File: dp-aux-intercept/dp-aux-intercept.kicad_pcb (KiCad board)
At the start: 2 copper layers, 24 parts

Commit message: Small fixes.
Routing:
- net /DCFG2: track 7.76 -> 14.6 mm
- net /DCFG1: track 4.83 -> 11.0 mm
- net /DHPD: track 32.4 -> 34.9 mm
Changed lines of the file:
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@@
-(kicad_pcb (version 4) (host pcbnew 0.201506030104+5696~23~ubuntu14.04.1-product)
+(kicad_pcb (version 4) (host pcbnew 0.201506252249+5822~23~ubuntu14.04.1-product)
   (general
     (links 86)
@@
     (thickness 1.6)
     (drawings 2)
-    (tracks 570)
+    (tracks 583)
     (zones 0)
     (modules 24)
@@
   (segment (start 42.418 70.74408) (end 42.418 63.73876) (width 0.15) (layer F.Cu) (net 3))
   (segment (start 45.20692 73.533) (end 42.418 70.74408) (width 0.15) (layer F.Cu) (net 3))
+  (segment (start 31.742 32.31) (end 32.467001 33.035001) (width 0.15) (layer F.Cu) (net 4))
+  (segment (start 32.467001 33.035001) (end 36.083001 33.035001) (width 0.15) (layer F.Cu) (net 4))
+  (segment (start 36.083001 33.035001) (end 36.78399 33.73599) (width 0.15) (layer F.Cu) (net 4))
+  (segment (start 36.78399 33.73599) (end 36.78399 34.24399) (width 0.15) (layer F.Cu) (net 4))
+  (segment (start 36.78399 34.24399) (end 36.83 34.29) (width 0.15) (layer F.Cu) (net 4))
   (segment (start 35.1917 51.43246) (end 34.1757 51.43246) (width 0.15) (layer F.Cu) (net 4))
   (segment (start 35.1917 55.24246) (end 35.1917 51.43246) (width 0.15) (layer F.Cu) (net 4))
+  (segment (start 37.084 34.036) (end 37.338 34.29) (width 0.15) (layer F.Cu) (net 5))
+  (segment (start 37.084 33.578998) (end 37.084 34.036) (width 0.15) (layer F.Cu) (net 5))
+  (segment (start 32.242 30.81) (end 33.016999 31.584999) (width 0.15) (layer F.Cu) (net 5))
+  (segment (start 33.016999 31.584999) (end 35.090001 31.584999) (width 0.15) (layer F.Cu) (net 5))
+  (segment (start 35.090001 31.584999) (end 37.084 33.578998) (width 0.15) (layer F.Cu) (net 5))
   (segment (start 37.7317 51.43246) (end 36.643099 50.343859) (width 0.15) (layer F.Cu) (net 5))
   (segment (start 36.643099 50.343859) (end 34.230099 50.343859) (width 0.15) (layer F.Cu) (net 5))
   (segment (start 37.7317 55.24246) (end 37.7317 54.021146) (width 0.15) (layer F.Cu) (net 5))
   (segment (start 37.7317 54.021146) (end 37.7317 51.43246) (width 0.15) (layer F.Cu) (net 5))
+  (segment (start 36.322 33.87402) (end 36.322 34.29) (width 0.15) (layer F.Cu) (net 6))
+  (segment (start 36.25798 33.81) (end 36.322 33.87402) (width 0.15) (layer F.Cu) (net 6))
+  (segment (start 34.242 33.81) (end 36.25798 33.81) (width 0.15) (layer F.Cu) (net 6))
   (segment (start 40.2717 51.43246) (end 38.820301 49.981061) (width 0.15) (layer F.Cu) (net 6))
   (segment (start 38.820301 49.981061) (end 34.669171 49.981061) (width 0.15) (layer F.Cu) (net 6))

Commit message: Temp commit.
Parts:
- RCCFG1: renamed from RCCFG2; value 5M -> 1M
- RCCFG2: renamed from RCHPD1; value 100K -> 5M
- RCHPD1: renamed from RCCFG1; value 1M -> 100K
- RDCFG1: renamed from RDCFG2; value 5M -> 1M
- RDCFG2: renamed from RDHPD1; value 100K -> 5M
- RDHPD1: renamed from RDCFG1; value 1M -> 100K
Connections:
- net Net-(JCCFG1-Pad2) renamed /JCHPD
- net Net-(JCCFG1-Pad4) renamed /JCCFG1
- net Net-(JCCFG1-Pad6) renamed /JCCFG2
- net Net-(JDCFG1-Pad2) renamed /JDHPD
- net Net-(JDCFG1-Pad4) renamed /JDCFG1
- net Net-(JDCFG1-Pad6) renamed /JDCFG2
- JCCFG1 pad 1: /CCFG1 -> /CHPD
- JCCFG1 pad 3: /CCFG2 -> /CCFG1
- JCCFG1 pad 5: /CHPD -> /CCFG2
- JDCFG1 pad 1: /DCFG1 -> /DHPD
- JDCFG1 pad 3: /DCFG2 -> /DCFG1
- JDCFG1 pad 5: /DHPD -> /DCFG2
- PCFG1 pad 1: /CCFG1 -> /CHPD
- PCFG1 pad 2: /DCFG1 -> /DHPD
- PCFG1 pad 3: /CCFG2 -> /CCFG1
- PCFG1 pad 4: /DCFG2 -> /DCFG1
- PCFG1 pad 5: /CHPD -> /CCFG2
- PCFG1 pad 6: /DHPD -> /DCFG2
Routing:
- net /DHPD: track 34.9 -> 50.9 mm
- net /DCFG1: track 11.0 -> 26.7 mm
- net /DCFG2: track 14.6 -> 29.0 mm
- net /CHPD: track 17.8 -> 28.3 mm
- net VDD: track 112.8 -> 116.5 mm
- net /CCFG2: track 6.74 -> 10.3 mm
- net /CCFG1: track 6.21 -> 9.25 mm

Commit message: Temp commit.
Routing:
- net /DAUX1_P: track 47.1 -> 44.8 mm
- net /DAUX1_N: track 50.6 -> 48.6 mm
- net VDD: track 116.5 -> 118.3 mm
- net /DCFG2: track 29.0 -> 29.6 mm, vias 0 -> 1
- net /DCFG1: track 26.7 -> 27.0 mm, vias 0 -> 1

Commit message: More temp commit.
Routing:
- net /CCFG1: track 9.25 -> 33.6 mm
- net /CCFG2: track 10.3 -> 34.2 mm
- net /CHPD: track 28.3 -> 26.9 mm
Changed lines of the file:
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@@
   (general
     (links 86)
-    (no_connects 29)
+    (no_connects 30)
     (area 22.242 18.23 58.531921 98.968)
     (thickness 1.6)
     (drawings 2)
-    (tracks 593)
+    (tracks 607)
     (zones 0)
     (modules 24)
@@
   (gr_line (start 32.004 82.55) (end 32.004 34.798) (layer B.SilkS) (width 0.2))
   (gr_line (start 32.004 34.798) (end 32.004 82.55) (layer F.SilkS) (width 0.2))
+  (segment (start 36.280301 71.403421) (end 36.280301 63.043859) (width 0.15) (layer F.Cu) (net 1))
+  (segment (start 32.467001 84.312999) (end 34.540003 84.312999) (width 0.15) (layer F.Cu) (net 1))
+  (segment (start 38.745549 77.395093) (end 38.745549 73.868669) (width 0.15) (layer F.Cu) (net 1))
+  (segment (start 36.957 78.1685) (end 37.435419 77.690081) (width 0.15) (layer F.Cu) (net 1))
+  (segment (start 36.280301 63.043859) (end 36.868101 62.456059) (width 0.15) (layer F.Cu) (net 1))
+  (segment (start 34.540003 84.312999) (end 36.957 81.896002) (width 0.15) (layer F.Cu) (net 1))
+  (segment (start 36.957 81.896002) (end 36.957 78.1685) (width 0.15) (layer F.Cu) (net 1))
+  (segment (start 31.742 85.038) (end 32.467001 84.312999) (width 0.15) (layer F.Cu) (net 1))
+  (segment (start 36.868101 62.456059) (end 37.7317 61.59246) (width 0.15) (layer F.Cu) (net 1))
+  (segment (start 37.435419 77.690081) (end 38.450561 77.690081) (width 0.15) (layer F.Cu) (net 1))
+  (segment (start 38.450561 77.690081) (end 38.745549 77.395093) (width 0.15) (layer F.Cu) (net 1))
+  (segment (start 38.745549 73.868669) (end 36.280301 71.403421) (width 0.15) (layer F.Cu) (net 1))
   (segment (start 37.7317 61.59246) (end 37.7317 57.78246) (width 0.15) (layer B.Cu) (net 1))
-  (segment (start 35.8394 83.693) (end 35.8394 82.9056) (width 0.15) (layer F.Cu) (net 1))
-  (segment (start 35.219401 84.312999) (end 35.8394 83.693) (width 0.15) (layer F.Cu) (net 1))
-  (segment (start 31.742 85.038) (end 32.467001 84.312999) (width 0.15) (layer F.Cu) (net 1))
-  (segment (start 32.467001 84.312999) (end 35.219401 84.312999) (width 0.15) (layer F.Cu) (net 1))
+  (segment (start 32.242 86.538) (end 33.016999 85.763001) (width 0.15) (layer F.Cu) (net 2))
+  (segment (start 33.016999 85.763001) (end 35.090001 85.763001) (width 0.15) (layer F.Cu) (net 2))
+  (segment (start 35.090001 85.763001) (end 37.353919 83.499083) (width 0.15) (layer F.Cu) (net 2))
+  (segment (start 37.353919 78.315999) (end 37.525919 78.143999) (width 0.15) (layer F.Cu) (net 2))
+  (segment (start 37.353919 83.499083) (end 37.353919 78.315999) (width 0.15) (layer F.Cu) (net 2))
+  (segment (start 37.525919 78.143999) (end 38.696001 78.143999) (width 0.15) (layer F.Cu) (net 2))
+  (segment (start 39.045559 77.794441) (end 39.045559 76.035079) (width 0.15) (layer F.Cu) (net 2))
+  (segment (start 38.696001 78.143999) (end 39.045559 77.794441) (width 0.15) (layer F.Cu) (net 2))
+  (segment (start 39.045559 76.035079) (end 39.24808 75.832558) (width 0.15) (layer F.Cu) (net 2))
+  (segment (start 39.24808 75.832558) (end 39.24554 75.830018) (width 0.15) (layer F.Cu) (net 2))
+  (segment (start 39.0017 62.86246) (end 40.2717 61.59246) (width 0.15) (layer F.Cu) (net 2))
+  (segment (start 39.24554 75.830018) (end 39.24554 65.45834) (width 0.15) (layer F.Cu) (net 2))
+  (segment (start 39.24554 65.45834) (end 39.0017 65.2145) (width 0.15) (layer F.Cu) (net 2))
+  (segment (start 39.0017 65.2145) (end 39.0017 62.86246) (width 0.15) (layer F.Cu) (net 2))
   (segment (start 40.2717 57.78246) (end 40.2717 61.59246) (width 0.15) (layer B.Cu) (net 2))
-  (segment (start 36.195 84.658002) (end 36.195 82.8802) (width 0.15) (layer F.Cu) (net 2))
-  (segment (start 32.242 86.538) (end 32.967001 85.812999) (width 0.15) (layer F.Cu) (net 2))
-  (segment (start 32.967001 85.812999) (end 35.040003 85.812999) (width 0.15) (layer F.Cu) (net 2))
-  (segment (start 35.040003 85.812999) (end 36.195 84.658002) (width 0.15) (layer F.Cu) (net 2))
   (segment (start 42.164 60.325) (end 42.164 70.49008) (width 0.15) (layer F.Cu) (net 3))
   (segment (start 42.164 70.49008) (end 45.20692 73.533) (width 0.15) (layer F.Cu) (net 3))
@@
   (segment (start 35.1917 57.78246) (end 35.1917 58.79606) (width 0.15) (layer F.Cu) (net 3))
   (segment (start 35.1917 58.79606) (end 35.83164 59.436) (width 0.15) (layer F.Cu) (net 3))
-  (segment (start 35.249799 83.038001) (end 35.3822 82.9056) (width 0.15) (layer F.Cu) (net 3))
-  (segment (start 34.242 83.538) (end 34.741999 83.038001) (width 0.15) (layer F.Cu) (net 3))
-  (segment (start 34.741999 83.038001) (end 35.249799 83.038001) (width 0.15) (layer F.Cu) (net 3))
   (segment (start 35.1917 61.59246) (end 35.1917 57.78246) (width 0.15) (layer F.Cu) (net 3))
   (segment (start 35.7505 33.5915) (end 36.643099 34.484099) (width 0.15) (layer F.Cu) (net 4))
   (segment (start 36.643099 34.484099) (end 36.643099 34.992099) (width 0.15) (layer F.Cu) (net 4))
+  (segment (start 36.643099 34.992099) (end 36.50742 35.127778) (width 0.15) (layer F.Cu) (net 4))
+  (segment (start 36.50742 35.127778) (end 36.50742 50.20818) (width 0.15) (layer F.Cu) (net 4))
+  (segment (start 36.50742 50.20818) (end 37.7317 51.43246) (width 0.15) (layer F.Cu) (net 4))
   (segment (start 31.742 32.31) (end 32.467001 33.035001) (width 0.15) (layer B.Cu) (net 4))
   (segment (start 32.467001 33.035001) (end 35.194001 33.035001) (width 0.15) (layer B.Cu) (net 4))
   (segment (start 35.194001 33.035001) (end 35.7505 33.5915) (width 0.15) (layer B.Cu) (net 4))
   (via (at 35.7505 33.5915) (size 0.6) (drill 0.3) (layers F.Cu B.Cu) (net 4))
-  (segment (start 36.643099 50.343859) (end 37.7317 51.43246) (width 0.15) (layer F.Cu) (net 4))
-  (segment (start 36.643099 34.992099) (end 36.643099 50.343859) (width 0.15) (layer F.Cu) (net 4))
   (segment (start 37.7317 55.24246) (end 37.7317 54.021146) (width 0.15) (layer F.Cu) (net 4))
   (segment (start 37.7317 54.021146) (end 37.7317 51.43246) (width 0.15) (layer F.Cu) (net 4))
-  (segment (start 36.634438 33.129436) (end 39.0144 35.509398) (width 0.15) (layer F.Cu) (net 5))
-  (segment (start 36.6395 32.3215) (end 36.6395 32.745764) (width 0.15) (layer F.Cu) (net 5))
-  (segment (start 36.6395 32.745764) (end 36.634438 32.750826) (width 0.15) (layer F.Cu) (net 5))
-  (segment (start 36.634438 32.750826) (end 36.634438 33.129436) (width 0.15) (layer F.Cu) (net 5))
+  (segment (start 36.6395 32.3215) (end 36.6395 33.134498) (width 0.15) (layer F.Cu) (net 5))
+  (segment (start 36.6395 33.134498) (end 39.0144 35.509398) (width 0.15) (layer F.Cu) (net 5))
+  (segment (start 39.0144 35.509398) (end 39.0144 50.17516) (width 0.15) (layer F.Cu) (net 5))
+  (segment (start 39.0144 50.17516) (end 40.2717 51.43246) (width 0.15) (layer F.Cu) (net 5))
   (segment (start 36.6395 32.131) (end 36.6395 32.3215) (width 0.15) (layer B.Cu) (net 5))
   (via (at 36.6395 32.3215) (size 0.6) (drill 0.3) (layers F.Cu B.Cu) (net 5))
@@
   (segment (start 32.242 30.81) (end 33.016999 31.584999) (width 0.15) (layer B.Cu) (net 5))
   (segment (start 33.016999 31.584999) (end 36.093499 31.584999) (width 0.15) (layer B.Cu) (net 5))
-  (segment (start 39.0144 35.509398) (end 39.0144 50.17516) (width 0.15) (layer F.Cu) (net 5))
-  (segment (start 39.0144 50.17516) (end 40.2717 51.43246) (width 0.15) (layer F.Cu) (net 5))
   (segment (start 40.2717 55.24246) (end 40.2717 51.43246) (width 0.15) (layer F.Cu) (net 5))
   (segment (start 47.74692 73.533) (end 46.658319 72.444399) (width 0.15) (layer F.Cu) (net 6))
@@
   (segment (start 32.742 83.538) (end 35.254 81.026) (width 0.15) (layer F.Cu) (net 17))
   (segment (start 35.254 81.026) (end 35.97892 81.026) (width 0.15) (layer F.Cu) (net 17))
-  (segment (start 32.742 33.81) (end 32.742 34.517106) (width 0.15) (layer F.Cu) (net 18))
-  (segment (start 32.742 34.517106) (end 31.92749 35.331616) (width 0.15) (layer F.Cu) (net 18))
-  (segment (start 31.92749 35.331616) (end 31.92749 35.496166) (width 0.15) (layer F.Cu) (net 18))
   (segment (start 33.340896 75.606729) (end 31.9025 74.168333) (width 0.125) (layer F.Cu) (net 18))
   (segment (start 31.9025 74.168333) (end 31.9025 35.496166) (width 0.125) (layer F.Cu) (net 18))
+  (segment (start 31.92749 35.331616) (end 31.92749 35.496166) (width 0.15) (layer F.Cu) (net 18))
+  (segment (start 32.742 34.517106) (end 31.92749 35.331616) (width 0.15) (layer F.Cu) (net 18))
+  (segment (start 32.742 33.81) (end 32.742 34.517106) (width 0.15) (layer F.Cu) (net 18))
   (segment (start 37.35056 76.67008) (end 37.52056 76.84008) (width 0.15) (layer F.Cu) (net 18))
   (segment (start 35.53206 76.67008) (end 37.35056 76.67008) (width 0.15) (layer F.Cu) (net 18))
@@
   (segment (start 32.016999 34.108003) (end 32.016999 33.461999) (width 0.15) (layer F.Cu) (net 20))
   (segment (start 32.016999 33.461999) (end 32.516999 32.961999) (width 0.15) (layer F.Cu) (net 20))
+  (segment (start 33.71386 30.83814) (end 33.742 30.81) (width 0.15) (layer F.Cu) (net 20))
   (segment (start 32.516999 32.961999) (end 32.516999 31.961999) (width 0.15) (layer F.Cu) (net 20))
-  (segment (start 32.516999 31.961999) (end 33.168999 31.309999) (width 0.15) (layer F.Cu) (net 20))
-  (segment (start 33.168999 31.309999) (end 33.242001 31.309999) (width 0.15) (layer F.Cu) (net 20))
-  (segment (start 33.242001 31.309999) (end 33.742 30.81) (width 0.15) (layer F.Cu) (net 20))
+  (segment (start 33.640858 30.83814) (end 33.71386 30.83814) (width 0.15) (layer F.Cu) (net 20))
+  (segment (start 32.516999 31.961999) (end 33.640858 30.83814) (width 0.15) (layer F.Cu) (net 20))
   (segment (start 31.5975 74.294667) (end 31.5975 35.369834) (width 0.125) (layer F.Cu) (net 20))
   (segment (start 33.125229 75.822396) (end 31.5975 74.294667) (width 0.125) (layer F.Cu) (net 20))

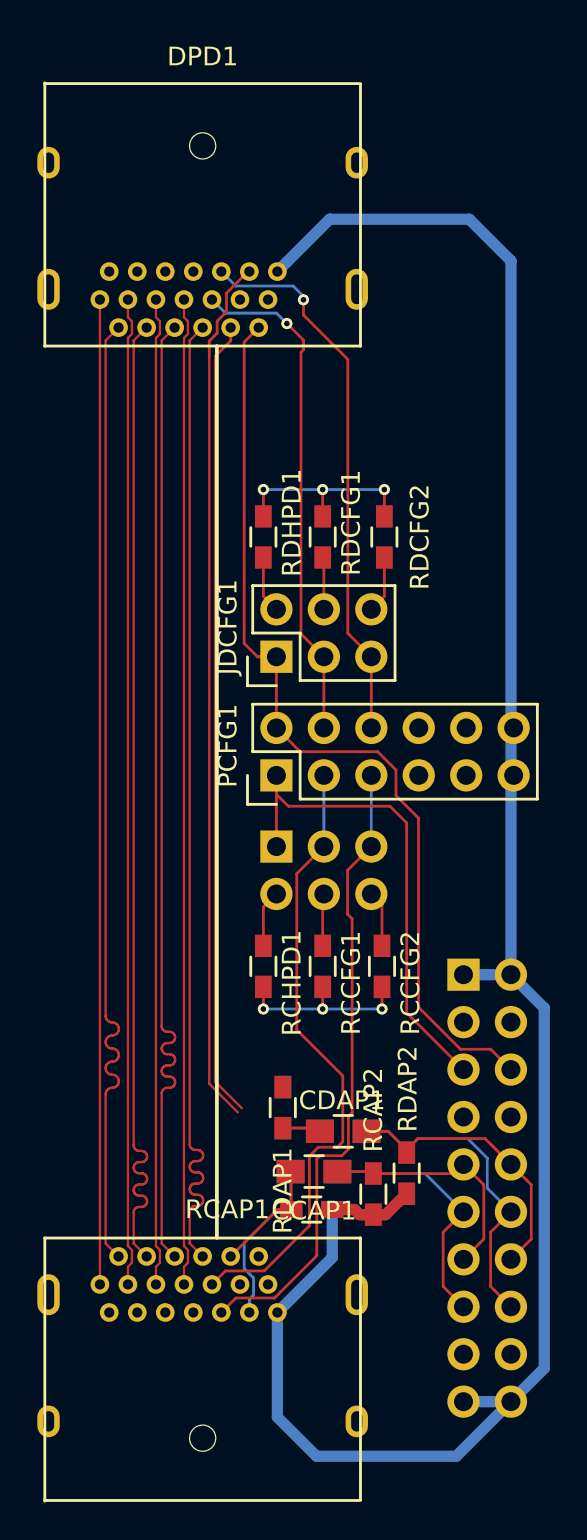
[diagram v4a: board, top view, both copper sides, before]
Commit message: Finishing connecting the traces.
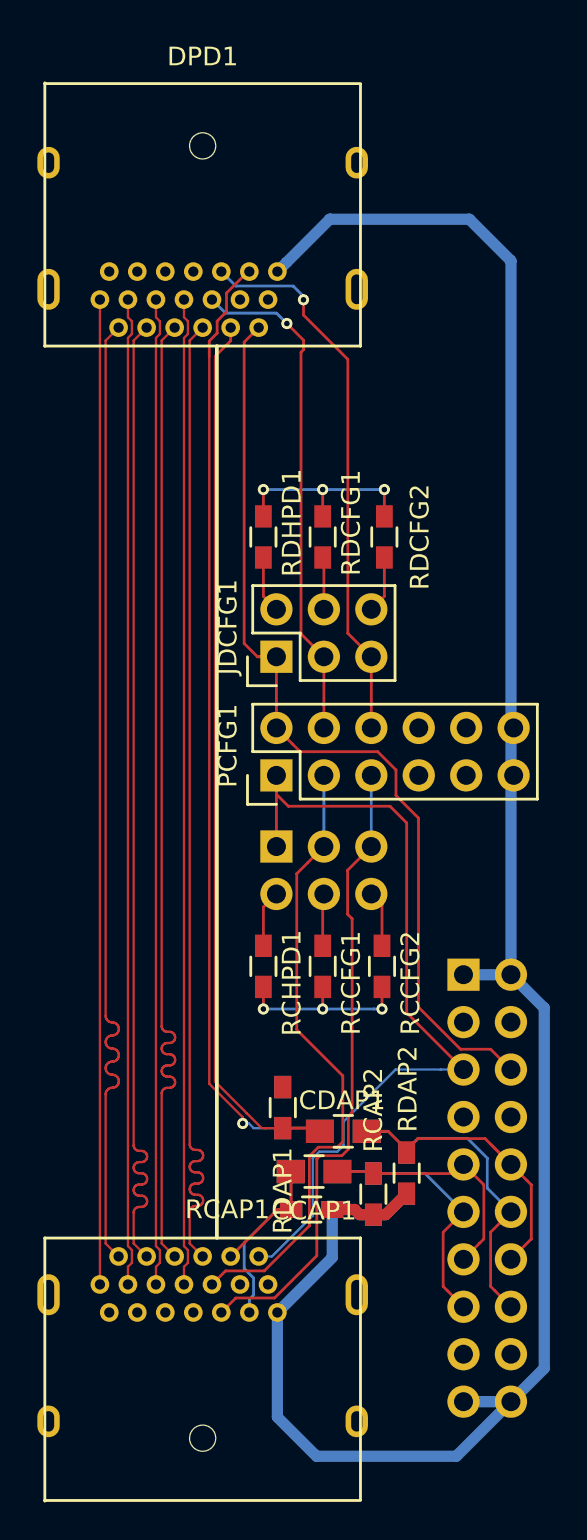
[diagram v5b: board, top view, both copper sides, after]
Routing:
- net /CHPD: track 26.9 -> 44.6 mm
- net /DAUX1_N: track 48.6 -> 51.6 mm, vias 0 -> 1
- net /DAUX1_P: track 44.8 -> 47.4 mm
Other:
- net class Default: trace_width 0.15 -> 0.125
- rule trace_min: 0.15 -> 0.125
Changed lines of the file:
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@@
-(kicad_pcb (version 4) (host pcbnew 0.201506252249+5822~23~ubuntu14.04.1-product)
+(kicad_pcb (version 4) (host pcbnew 4.0.2+e4-6225~38~ubuntu14.04.1-stable)
   (general
     (links 86)
-    (no_connects 30)
+    (no_connects 29)
     (area 22.242 18.23 58.531921 98.968)
     (thickness 1.6)
     (drawings 2)
-    (tracks 607)
+    (tracks 626)
     (zones 0)
     (modules 24)
@@
   (page A4)
   (layers
-    (0 F.Cu signal)
+    (0 F.Cu signal hide)
     (31 B.Cu signal)
     (32 B.Adhes user)
@@
   )
   (setup
-    (last_trace_width 0.15)
+    (last_trace_width 0.125)
+    (user_trace_width 0.125)
+    (user_trace_width 0.15)
     (trace_clearance 0.15)
     (zone_clearance 0.508)
     (zone_45_only no)
-    (trace_min 0.15)
+    (trace_min 0.125)
     (segment_width 0.2)
     (edge_width 0.1)
@@
   (net_class Default "This is the default net class."
     (clearance 0.15)
-    (trace_width 0.15)
+    (trace_width 0.125)
     (via_dia 0.6)
     (via_drill 0.3)
@@
   (segment (start 39.0017 65.2145) (end 39.0017 62.86246) (width 0.15) (layer F.Cu) (net 2))
   (segment (start 40.2717 57.78246) (end 40.2717 61.59246) (width 0.15) (layer B.Cu) (net 2))
+  (segment (start 34.242 83.538) (end 34.949106 83.538) (width 0.125) (layer B.Cu) (net 3))
+  (segment (start 34.949106 83.538) (end 37.1348 81.352306) (width 0.125) (layer B.Cu) (net 3))
+  (segment (start 37.1348 81.352306) (end 37.1348 78.2828) (width 0.125) (layer B.Cu) (net 3))
+  (segment (start 38.4556 77.9272) (end 38.7858 77.597) (width 0.125) (layer B.Cu) (net 3))
+  (segment (start 43.985606 73.533) (end 45.20692 73.533) (width 0.125) (layer B.Cu) (net 3))
+  (segment (start 37.1348 78.2828) (end 37.4904 77.9272) (width 0.125) (layer B.Cu) (net 3))
+  (segment (start 38.7858 77.597) (end 38.7858 76.317338) (width 0.125) (layer B.Cu) (net 3))
+  (segment (start 37.4904 77.9272) (end 38.4556 77.9272) (width 0.125) (layer B.Cu) (net 3))
+  (segment (start 38.7858 76.317338) (end 41.570138 73.533) (width 0.125) (layer B.Cu) (net 3))
+  (segment (start 41.570138 73.533) (end 43.985606 73.533) (width 0.125) (layer B.Cu) (net 3))
   (segment (start 42.164 60.325) (end 42.164 70.49008) (width 0.15) (layer F.Cu) (net 3))
   (segment (start 42.164 70.49008) (end 45.20692 73.533) (width 0.15) (layer F.Cu) (net 3))
@@
   (segment (start 32.742 83.538) (end 35.254 81.026) (width 0.15) (layer F.Cu) (net 17))
   (segment (start 35.254 81.026) (end 35.97892 81.026) (width 0.15) (layer F.Cu) (net 17))
-  (segment (start 33.340896 75.606729) (end 31.9025 74.168333) (width 0.125) (layer F.Cu) (net 18))
-  (segment (start 31.9025 74.168333) (end 31.9025 35.496166) (width 0.125) (layer F.Cu) (net 18))
+  (segment (start 33.601479 75.867079) (end 34.40448 76.67008) (width 0.125) (layer F.Cu) (net 18))
+  (segment (start 34.40448 76.67008) (end 35.53206 76.67008) (width 0.125) (layer F.Cu) (net 18))
+  (segment (start 33.601246 75.867079) (end 33.601479 75.867079) (width 0.125) (layer F.Cu) (net 18))
+  (segment (start 31.9025 35.496166) (end 31.9025 74.168333) (width 0.125) (layer F.Cu) (net 18))
+  (segment (start 31.9025 74.168333) (end 33.601246 75.867079) (width 0.125) (layer F.Cu) (net 18))
   (segment (start 31.92749 35.331616) (end 31.92749 35.496166) (width 0.15) (layer F.Cu) (net 18))
   (segment (start 32.742 34.517106) (end 31.92749 35.331616) (width 0.15) (layer F.Cu) (net 18))
@@
   (segment (start 33.467001 82.814199) (end 35.2552 81.026) (width 0.15) (layer B.Cu) (net 19))
   (segment (start 35.2552 81.026) (end 35.97892 81.026) (width 0.15) (layer B.Cu) (net 19))
+  (segment (start 33.385579 76.418621) (end 33.721454 76.418621) (width 0.125) (layer B.Cu) (net 20))
+  (segment (start 33.721454 76.418621) (end 33.972913 76.67008) (width 0.125) (layer B.Cu) (net 20))
+  (segment (start 33.972913 76.67008) (end 34.625678 76.67008) (width 0.125) (layer B.Cu) (net 20))
+  (segment (start 34.625678 76.67008) (end 35.53206 76.67008) (width 0.125) (layer B.Cu) (net 20))
+  (segment (start 33.385579 76.082746) (end 33.385579 76.418621) (width 0.125) (layer F.Cu) (net 20))
+  (via (at 33.385579 76.418621) (size 0.6) (drill 0.3) (layers F.Cu B.Cu) (net 20))
+  (segment (start 31.5975 74.294667) (end 33.385579 76.082746) (width 0.125) (layer F.Cu) (net 20))
+  (segment (start 31.5975 35.369834) (end 31.5975 74.294667) (width 0.125) (layer F.Cu) (net 20))
   (segment (start 31.5975 35.369834) (end 31.5975 34.527502) (width 0.15) (layer F.Cu) (net 20))
   (segment (start 31.5975 34.527502) (end 32.016999 34.108003) (width 0.15) (layer F.Cu) (net 20))
@@
   (segment (start 33.640858 30.83814) (end 33.71386 30.83814) (width 0.15) (layer F.Cu) (net 20))
   (segment (start 32.516999 31.961999) (end 33.640858 30.83814) (width 0.15) (layer F.Cu) (net 20))
-  (segment (start 31.5975 74.294667) (end 31.5975 35.369834) (width 0.125) (layer F.Cu) (net 20))
-  (segment (start 33.125229 75.822396) (end 31.5975 74.294667) (width 0.125) (layer F.Cu) (net 20))
   (segment (start 37.35056 76.67008) (end 37.52056 76.84008) (width 0.15) (layer B.Cu) (net 20))
   (segment (start 35.53206 76.67008) (end 37.35056 76.67008) (width 0.15) (layer B.Cu) (net 20))
